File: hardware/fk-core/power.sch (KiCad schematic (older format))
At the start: 43 parts, among them CN1 DCBARRELSMT, CN2 JST_2PIN-SMT, P1 USB_OTG, P3 CONN_01X02, P4 CONN_01X02, P6 CONN_01X02, P7 CONN_01X02, U2 MCP73871, U3 INA219, U4 INA219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

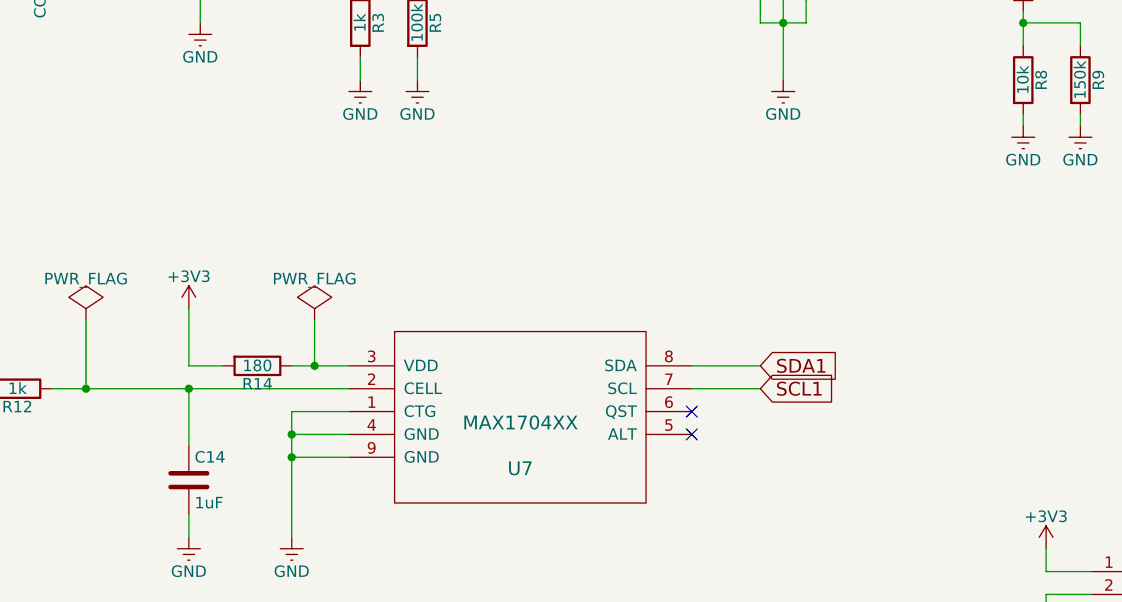
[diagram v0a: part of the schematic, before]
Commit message: Some footprints, cleaning things up.
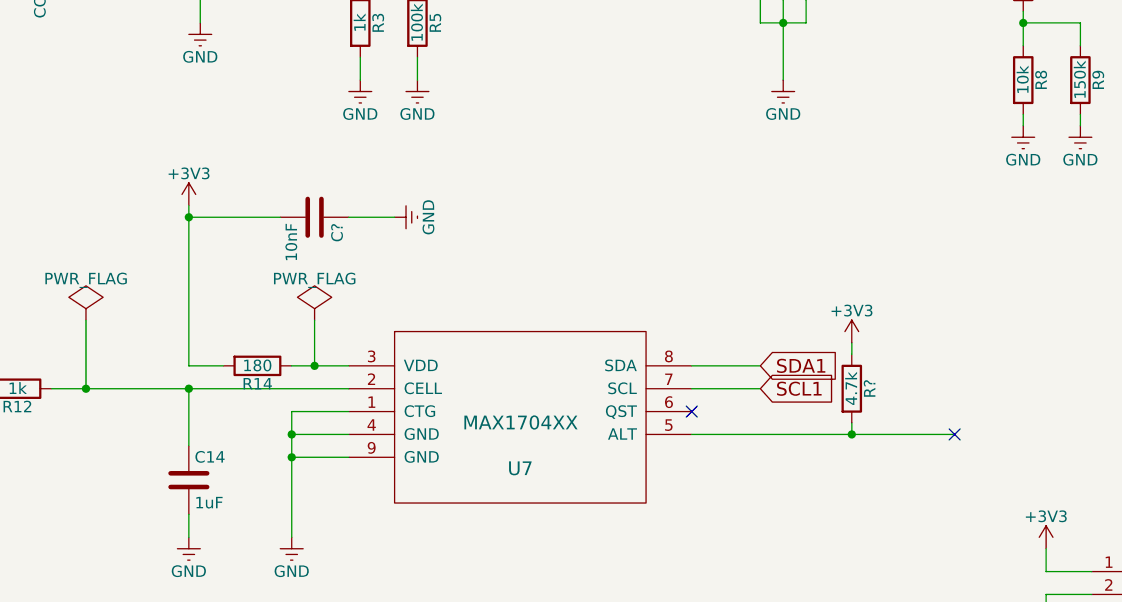
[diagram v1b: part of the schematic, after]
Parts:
- added C?: 10nF, symbol C
- added R?: 4.7k, symbol R
- U7: SPN2 (none) -> BQ28Z610
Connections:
- wire segments 169 -> 174
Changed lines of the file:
@@
 F 3 "http://datasheets.maximintegrated.com/en/ds/MAX17043-MAX17044.pdf" H 3750 4800 60  0001 C CNN
 F 4 "MAX17043G+T-ND" H 3750 4800 60  0001 C CNN "SPN"
+F 5 "BQ28Z610" H 3750 4800 60  0001 C CNN "SPN2"
 	1    3750 4800
 	1    0    0    -1
@@
 L +3V3 #PWR048
 U 1 1 58803F8C
-P 2300 4300
-F 0 "#PWR048" H 2300 4150 50  0001 C CNN
-F 1 "+3V3" H 2300 4440 50  0000 C CNN
-F 2 "" H 2300 4300 50  0000 C CNN
-F 3 "" H 2300 4300 50  0000 C CNN
-	1    2300 4300
+P 2300 3850
+F 0 "#PWR048" H 2300 3700 50  0001 C CNN
+F 1 "+3V3" H 2300 3990 50  0000 C CNN
+F 2 "" H 2300 3850 50  0000 C CNN
+F 3 "" H 2300 3850 50  0000 C CNN
+	1    2300 3850
 	1    0    0    -1
 $EndComp
@@
 $EndComp
 Wire Wire Line
-	2450 4550 2300 4550
-Wire Wire Line
-	2300 4550 2300 4300
+	2300 4550 2450 4550
+Wire Wire Line
+	2300 3850 2300 4550
 $Comp
 L C C14
@@
 	4500 4550 4800 4550
 NoConn ~ 4500 4750
-NoConn ~ 4500 4850
 Wire Wire Line
 	2650 7400 2650 7350
@@
 	1    0    0    -1
 $EndComp
+$Comp
+L C C?
+U 1 1 58817F74
+P 2850 3900
+F 0 "C?" H 2875 4000 50  0000 L CNN
+F 1 "10nF" H 2875 3800 50  0000 L CNN
+F 2 "" H 2888 3750 50  0000 C CNN
+F 3 "" H 2850 3900 50  0000 C CNN
+F 4 "490-1313-1-ND" H 2850 3900 60  0001 C CNN "SPN"
+	1    2850 3900
+	0    1    1    0
+$EndComp
+Wire Wire Line
+	2700 3900 2300 3900
+Connection ~ 2300 3900
+$Comp
+L GND #PWR?
+U 1 1 588182B4
+P 3200 3900
+F 0 "#PWR?" H 3200 3650 50  0001 C CNN
+F 1 "GND" H 3200 3750 50  0000 C CNN
+F 2 "" H 3200 3900 50  0000 C CNN
+F 3 "" H 3200 3900 50  0000 C CNN
+	1    3200 3900
+	0    -1   -1   0
+$EndComp
+Wire Wire Line
+	3200 3900 3000 3900
+$Comp
+L R R?
+U 1 1 588190EB
+P 5200 4650
+F 0 "R?" V 5280 4650 50  0000 C CNN
+F 1 "4.7k" V 5200 4650 50  0000 C CNN
+F 2 "" V 5130 4650 50  0000 C CNN
+F 3 "" H 5200 4650 50  0000 C CNN
+F 4 "541-4.70KCCT-ND" V 5200 4650 60  0001 C CNN "SPN"
+	1    5200 4650
+	1    0    0    -1
+$EndComp
+Wire Wire Line
+	4500 4850 5650 4850
+$Comp
+L +3V3 #PWR?
+U 1 1 5881AA8A
+P 5200 4450
+F 0 "#PWR?" H 5200 4300 50  0001 C CNN
+F 1 "+3V3" H 5200 4590 50  0000 C CNN
+F 2 "" H 5200 4450 50  0000 C CNN
+F 3 "" H 5200 4450 50  0000 C CNN
+	1    5200 4450
+	1    0    0    -1
+$EndComp
+Wire Wire Line
+	5200 4450 5200 4500
+Wire Wire Line
+	5200 4850 5200 4800
+Connection ~ 5200 4850
+NoConn ~ 5650 4850
 $EndSCHEMATC
